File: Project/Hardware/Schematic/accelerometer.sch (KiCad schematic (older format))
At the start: 1 part, among them U3 LSM303C

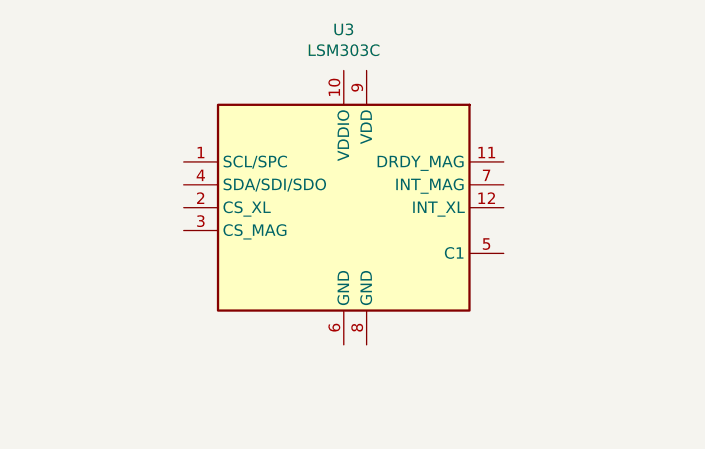
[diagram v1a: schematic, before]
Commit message: Accelerometer footprint
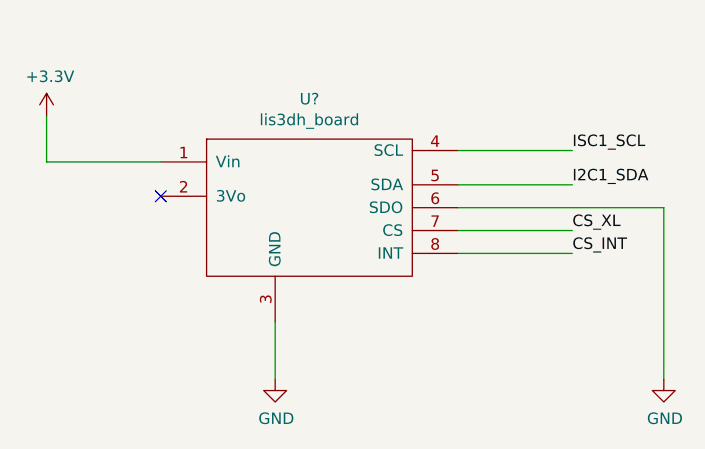
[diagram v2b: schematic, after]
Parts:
- removed U3: LSM303C, PASC:LGA-12_2x2mm_Pitch0.5mm_Handsolder, symbol Sensor_Motion:LSM303C
- added U?: lis3dh_board, symbol PASC:lis3dh_board
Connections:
- new net +3V3: U?.1 (Vin)
- new net CS_INT: U?.8 (INT)
- new net CS_XL: U?.7 (CS)
- new net GND: U?.3 (GND), U?.6 (SDO)
- new net I2C1_SDA: U?.5 (SDA)
- new net ISC1_SCL: U?.4 (SCL)
- no-connect marks 0 -> 1
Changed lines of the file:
@@
 $EndDescr
 $Comp
-L Sensor_Motion:LSM303C U3
-U 1 1 5C5615EE
-P 7500 3350
-F 0 "U3" H 7500 4128 50  0000 C CNN
-F 1 "LSM303C" H 7500 4037 50  0000 C CNN
-F 2 "PASC:LGA-12_2x2mm_Pitch0.5mm_Handsolder" H 7100 2650 50  0001 L CNN
-F 3 "www.st.com/resource/en/datasheet/lsm303c.pdf" H 7600 2700 50  0001 C CNN
-	1    7500 3350
+L power:+3.3V #PWR0120
+U 1 1 5C5AB0A3
+P 6200 2950
+F 0 "#PWR0120" H 6200 2800 50  0001 C CNN
+F 1 "+3.3V" H 6215 3123 50  0000 C CNN
+F 2 "" H 6200 2950 50  0001 C CNN
+F 3 "" H 6200 2950 50  0001 C CNN
+	1    6200 2950
 	1    0    0    -1
 $EndComp
+Wire Wire Line
+	6200 2950 6200 3150
+$Comp
+L PASC:lis3dh_board U?
+U 1 1 5C59F00B
+P 7350 3350
+F 0 "U?" H 7350 3825 50  0000 C CNN
+F 1 "lis3dh_board" H 7350 3734 50  0000 C CNN
+F 2 "" H 7350 3350 50  0001 C CNN
+F 3 "" H 7350 3350 50  0001 C CNN
+	1    7350 3350
+	1    0    0    -1
+$EndComp
+Wire Wire Line
+	6700 3150 6200 3150
+$Comp
+L power:GND #PWR?
+U 1 1 5C59F3FC
+P 7200 4100
+F 0 "#PWR?" H 7200 3850 50  0001 C CNN
+F 1 "GND" H 7205 3927 50  0000 C CNN
+F 2 "" H 7200 4100 50  0001 C CNN
+F 3 "" H 7200 4100 50  0001 C CNN
+	1    7200 4100
+	1    0    0    -1
+$EndComp
+Wire Wire Line
+	7200 3850 7200 4100
+$Comp
+L power:GND #PWR?
+U 1 1 5C59F76F
+P 8900 4100
+F 0 "#PWR?" H 8900 3850 50  0001 C CNN
+F 1 "GND" H 8905 3927 50  0000 C CNN
+F 2 "" H 8900 4100 50  0001 C CNN
+F 3 "" H 8900 4100 50  0001 C CNN
+	1    8900 4100
+	1    0    0    -1
+$EndComp
+Wire Wire Line
+	8900 3350 8900 4100
+NoConn ~ 6700 3300
+Wire Wire Line
+	8000 3100 8500 3100
+Text Label 8500 3100 0    50   ~ 0
+ISC1_SCL
+Wire Wire Line
+	8000 3250 8500 3250
+Text Label 8500 3250 0    50   ~ 0
+I2C1_SDA
+Wire Wire Line
+	8000 3350 8900 3350
+Wire Wire Line
+	8000 3550 8500 3550
+Text Label 8500 3550 0    50   ~ 0
+CS_INT
+Wire Wire Line
+	8000 3450 8500 3450
+Text Label 8500 3450 0    50   ~ 0
+CS_XL
 $EndSCHEMATC
